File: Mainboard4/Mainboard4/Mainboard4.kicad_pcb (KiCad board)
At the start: 2 copper layers, 145.9 x 180.3 mm, 41 parts, among them J0 Conn_01x18, J1 Conn_01x18, J2 Conn_01x18, J3 Conn_01x18, J4 Conn_01x18, J5 Conn_01x18, J7 Conn_01x02_Female, J8 Conn_01x12_Female, SW1 SW_DIP_x01, SW2 SW_DIP_x01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

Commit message: nearly ok
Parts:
- added C4: 0.1µF, Capacitor_THT:CP_Radial_Tantal_D5.0mm_P2.50mm, F.Cu at (142.4, 46.9)
- added C5: 10µF, Capacitor_THT:CP_Radial_Tantal_D5.0mm_P2.50mm, F.Cu at (137.0, 46.9)
- added J6: Conn_02x08_Odd_Even, Connector_PinHeader_2.54mm:PinHeader_2x08_P2.54mm_Vertical, F.Cu at (191.5, 96.3)
- added JP3: Jumper_2_Open, Connector_PinHeader_2.54mm:PinHeader_1x02_P2.54mm_Vertical, F.Cu at (118.0, 34.0)
- added JP4: Jumper_2_Open, Connector_PinHeader_2.54mm:PinHeader_1x02_P2.54mm_Vertical, F.Cu at (118.0, 38.2)
- added R10: R, Resistor_THT:R_Axial_DIN0207_L6.3mm_D2.5mm_P7.62mm_Horizontal, F.Cu at (191.5, 104.4)
- added R11: R, Resistor_THT:R_Axial_DIN0207_L6.3mm_D2.5mm_P7.62mm_Horizontal, F.Cu at (189.0, 104.4)
- added R12: R, Resistor_THT:R_Axial_DIN0207_L6.3mm_D2.5mm_P7.62mm_Horizontal, F.Cu at (186.4, 104.4)
- added R13: R, Resistor_THT:R_Axial_DIN0207_L6.3mm_D2.5mm_P7.62mm_Horizontal, F.Cu at (183.9, 104.4)
- added R14: R, Resistor_THT:R_Axial_DIN0207_L6.3mm_D2.5mm_P7.62mm_Horizontal, F.Cu at (181.4, 104.4)
- added R15: R, Resistor_THT:R_Axial_DIN0207_L6.3mm_D2.5mm_P7.62mm_Horizontal, F.Cu at (178.8, 104.4)
- added R16: R, Resistor_THT:R_Axial_DIN0207_L6.3mm_D2.5mm_P7.62mm_Horizontal, F.Cu at (176.3, 104.4)
- added R17: R, Resistor_THT:R_Axial_DIN0207_L6.3mm_D2.5mm_P7.62mm_Horizontal, F.Cu at (173.7, 104.4)
- added REF**: MountingHole_2.2mm_M2, MountingHole:MountingHole_2.2mm_M2, F.Cu at (61.0, 38.6)
- added REF**: MountingHole_2.2mm_M2, MountingHole:MountingHole_2.2mm_M2, F.Cu at (101.6, 169.4)
- added REF**: MountingHole_2.2mm_M2, MountingHole:MountingHole_2.2mm_M2, F.Cu at (194.3, 37.6)
- added REF**: MountingHole_2.2mm_M2, MountingHole:MountingHole_2.2mm_M2, F.Cu at (58.4, 206.4)
- added REF**: MountingHole_2.2mm_M2, MountingHole:MountingHole_2.2mm_M2, F.Cu at (102.2, 80.5)
- added REF**: MountingHole_2.2mm_M2, MountingHole:MountingHole_2.2mm_M2, F.Cu at (194.3, 199.4)
- added U7: ULN2803A, Package_DIP:DIP-18_W7.62mm, F.Cu at (191.5, 84.1)
- J_I2C_3: value Conn_01x04_Female -> Conn_01x06_Female; footprint Connector_PinHeader_2.54mm:PinHeader_1x04_P2.54mm_Vertical -> Connector_PinHeader_2.54mm:PinHeader_1x06_P2.54mm_Vertical
- moved C2 55.2 mm to (187.3, 47.2), turned to -90 degrees
- moved R5 38.5 mm to (120.3, 47.1), turned to 0 degrees
- moved JP1 36.5 mm to (189.2, 144.9), turned to 180 degrees
- moved J_POWER1 27.1 mm to (145.0, 34.0), turned to 90 degrees
- moved R9 20.7 mm to (192.7, 164.6)
- moved R2 20.2 mm to (165.1, 46.4), turned to 0 degrees
- moved R8 17.4 mm to (192.5, 150.0), turned to 90 degrees
- moved R4 17.3 mm to (127.9, 43.6), turned to 180 degrees
- moved U1 16.8 mm to (182.2, 42.6)
- moved SW1 14.6 mm to (168.4, 35.1), turned to -90 degrees
- moved C3 13.3 mm to (182.1, 47.2), turned to -90 degrees
- moved JP2 12.5 mm to (189.2, 168.1), turned to 0 degrees
- moved SW3 9.90 mm to (127.3, 34.0), turned to -90 degrees
- moved R3 8.07 mm to (176.5, 50.0), turned to 90 degrees
- moved R6 6.27 mm to (131.1, 49.0), turned to 90 degrees
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- renumbered J7 to J_POWER1
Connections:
- JP2 pad 1: Net-(JP1-Pad1) -> Net-(R9-Pad1)
- JP2 pad 2: Net-(JP2-Pad2) -> Net-(JP1-Pad1)
- J_GUI1 pad 1: unconnected-(J_GUI1-Pad1) -> 12V
- R9 pad 1: Net-(J_BUS1-Pad4) -> Net-(R9-Pad1)
- R9 pad 2: Net-(JP2-Pad2) -> Net-(J_BUS1-Pad4)
- SW3 pad 2: 12V -> Net-(SW3-Pad2)
- U2 pad 48: unconnected-(U2-Pad48) -> LED1
- U2 pad 63: LED4 -> LED8
- U2 pad 79: LED3 -> LED6
- U2 pad 83: unconnected-(U2-Pad83) -> LED5
- U2 pad 85: unconnected-(U2-Pad85) -> LED4
- U2 pad 87: unconnected-(U2-Pad87) -> LED3
- U2 pad 92: unconnected-(U2-Pad92) -> LED2
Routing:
- net 5V: track 133.1 -> 416.8 mm
- net 3V3: track 0.00 -> 234.5 mm, vias 0 -> 1
- net TRACK0_1: track 0.00 -> 125.0 mm
- net TRACK0_0: track 0.00 -> 123.8 mm
- net 12Vunreg: track 0.00 -> 107.9 mm
- net TRACK1_1: track 0.00 -> 103.4 mm
- net TRACK1_0: track 0.00 -> 101.5 mm
- net LED1: track 0.00 -> 82.3 mm
- net TRACK2_1: track 0.00 -> 78.4 mm
- net TRACK2_0: track 0.00 -> 74.1 mm
- net 12V: track 270.8 -> 343.2 mm
- net Net-(JP1-Pad1): track 0.00 -> 55.1 mm
- net TRACK3_1: track 0.00 -> 50.7 mm
- net Net-(J_BUS1-Pad4): track 0.18 -> 50.8 mm
- net TRACK3_0: track 0.00 -> 48.3 mm
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
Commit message: nearly ok
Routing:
- net GND: track 0.00 -> 87.1 mm, vias 0 -> 2
- net 3V3: track 234.5 -> 242.1 mm
- net 5V: track 416.8 -> 413.0 mm, vias 1 -> 2
- net CT0_3: track 85.4 -> 84.0 mm
- net CT1_3: track 48.2 -> 46.9 mm
- net CT5_1: track 125.9 -> 124.8 mm
- net VSENSE4_0: track 162.5 -> 161.7 mm
- net CT5_3: track 122.8 -> 122.0 mm
- net VSENSE3_1: track 136.4 -> 135.7 mm
- net CT0_2: track 64.7 -> 64.1 mm
- net PWM1_1: track 112.9 -> 112.2 mm
- net VSENSE5_0: track 191.7 -> 191.1 mm
- added copper zone on B.Cu, net GND
- added copper zone on F.Cu, net GND

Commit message: nearly ok
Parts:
- moved R10 2.16 mm to (193.7, 104.4)
- moved R17 1.65 mm to (172.1, 104.4)
- moved R11 1.52 mm to (190.5, 104.4)
- moved R16 1.02 mm to (175.3, 104.4)
- moved R12 0.89 mm to (187.3, 104.4)
- moved J_T5 0.64 mm to (183.1, 207.4)
- moved J_T6 0.64 mm to (195.3, 207.4)
- moved J_T1 0.63 mm to (171.4, 207.6)
- moved C2 0.38 mm to (187.7, 47.2)
- moved R15 0.38 mm to (178.4, 104.4)
- moved C4 0.30 mm to (142.7, 46.9)
- moved R13 0.25 mm to (184.2, 104.4)
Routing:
- net GND: track 87.1 -> 68.5 mm, vias 2 -> 0
- net Net-(J_T6-Pad1): track 46.9 -> 43.0 mm
- net 12V: track 343.2 -> 341.3 mm
- net 5V: track 413.0 -> 414.8 mm
- net CT1_3: track 46.9 -> 45.9 mm
- net Net-(J6-Pad2): track 5.59 -> 6.48 mm
- net Net-(J6-Pad16): track 5.59 -> 6.27 mm
- net Net-(J_T6-Pad3): track 39.3 -> 38.7 mm
- net Net-(J6-Pad4): track 5.59 -> 6.22 mm

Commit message: ..
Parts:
- moved C2 2.92 mm to (190.6, 47.2)
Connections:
- C1 pad 2: 5V -> 5VCPU
- C3 pad 1: Net-(R3-Pad1) -> 5V
- R3 pad 1: Net-(R3-Pad1) -> 5V
- SW1 pad 1: Net-(R3-Pad1) -> 5V
- SW1 pad 2: 5V -> 5VCPU
- U1 pad 2: Net-(R3-Pad1) -> 5V
- U2 pad 49: 5V -> 5VCPU
- U2 pad 50: 5V -> 5VCPU
- U2 pad 51: 5V -> 5VCPU
- U2 pad 52: 5V -> 5VCPU
- U4 pad 3: 5V -> 5VCPU
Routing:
- net 5VCPU: track 0.00 -> 194.8 mm, vias 0 -> 1
- net 5V: track 414.8 -> 222.3 mm, vias 2 -> 0
- net Net-(R3-Pad1): track 32.8 -> 0.00 mm
- net 12Vunreg: track 108.2 -> 109.8 mm

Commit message: mainboard4 ready for production
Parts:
- moved SW_12V1 28.7 mm to (98.6, 34.3)
- moved C2 18.3 mm to (172.3, 45.9)
- moved C5 18.3 mm to (118.7, 45.7)
- moved J_BUS1 18.3 mm to (178.1, 173.7)
- moved J_GUI1 18.3 mm to (178.1, 150.9)
- moved J_I2C_3_IUI1 18.3 mm to (178.1, 118.6)
- moved J_T1 18.3 mm to (153.1, 206.4)
- moved J_T2 18.3 mm to (139.8, 206.4)
- moved R1 18.3 mm to (154.4, 41.5)
- moved R10 18.3 mm to (175.4, 103.1)
- moved R11 18.3 mm to (172.2, 103.1)
- moved R13 18.3 mm to (165.9, 103.1)
- moved R15 18.3 mm to (160.1, 103.1)
- moved R17 18.3 mm to (153.8, 103.1)
- moved R3 18.3 mm to (158.2, 48.8)
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- renumbered J6 to J6_LEDS1, J_I2C_3 to J_I2C_3_IUI1, SW3 to SW_12V1, SW1 to SW_5VCPU1, SW2 to SW_GEN1
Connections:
- C5 pad 1: Net-(R6-Pad1) -> Net-(C5-Pad1)
- JP3 pad 1: Net-(SW3-Pad2) -> Net-(C5-Pad1)
- JP3 pad 2: 12V -> Net-(JP3-Pad2)
- JP4 pad 2: 12V -> Net-(JP3-Pad2)
- R6 pad 1: Net-(R6-Pad1) -> Net-(C5-Pad1)
- SW_12V1 pad 1: Net-(R6-Pad1) -> Net-(JP3-Pad2)
- SW_12V1 pad 2: Net-(SW3-Pad2) -> 12V
- U3 pad 2: Net-(R6-Pad1) -> Net-(C5-Pad1)
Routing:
- net Net-(C5-Pad1): track 0.00 -> 34.2 mm
- net Net-(R6-Pad1): track 29.5 -> 0.00 mm
- net 12Vunreg: track 109.8 -> 98.2 mm
- net Net-(JP3-Pad2): track 0.00 -> 11.2 mm
- net Net-(SW3-Pad2): track 6.73 -> 0.00 mm
- net 12V: track 341.3 -> 338.3 mm
- net 5VCPU: track 194.8 -> 195.3 mm
- net GND: vias 0 -> 3
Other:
- board text added: "Z-ATC Mainboard v0.4 © D. Braun 2022"
- board text removed: "Mainboard v0.4 © D. Braun 2022"

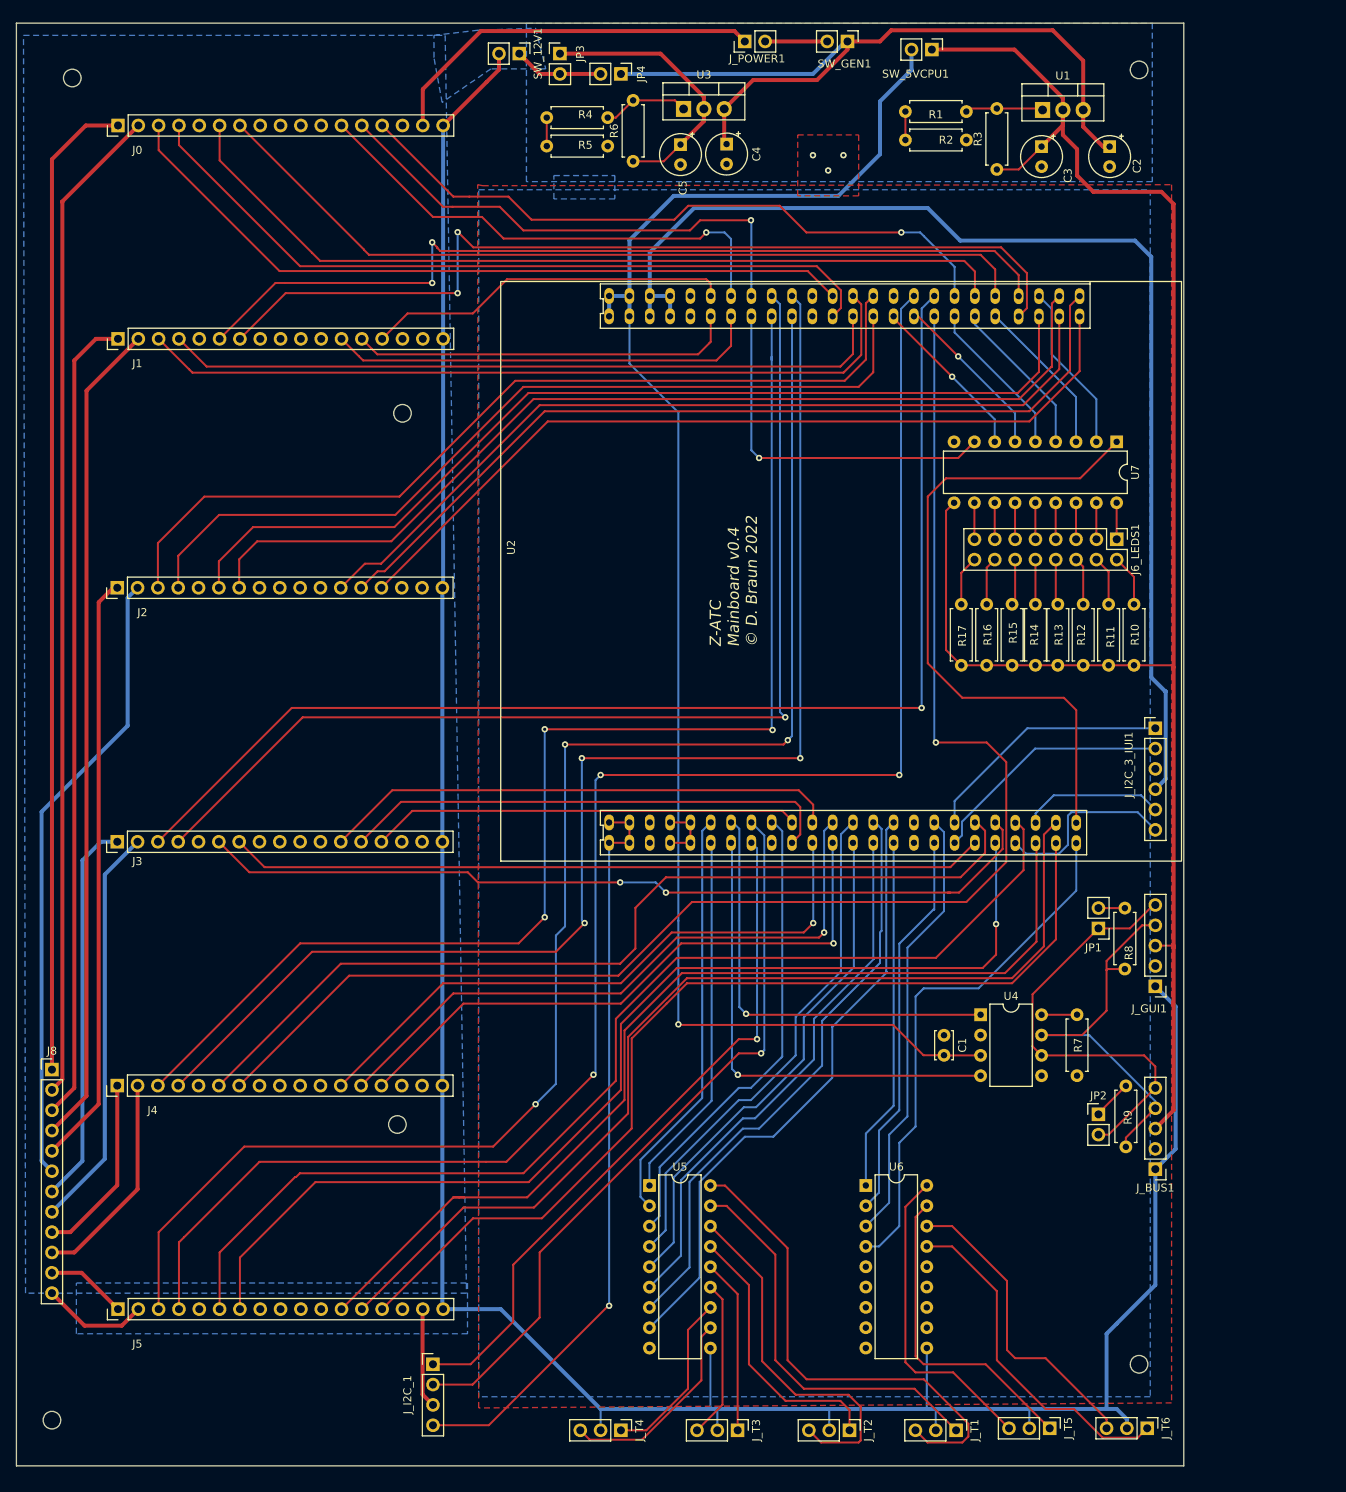
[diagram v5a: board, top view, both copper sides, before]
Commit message: updated to have full USB and external flash
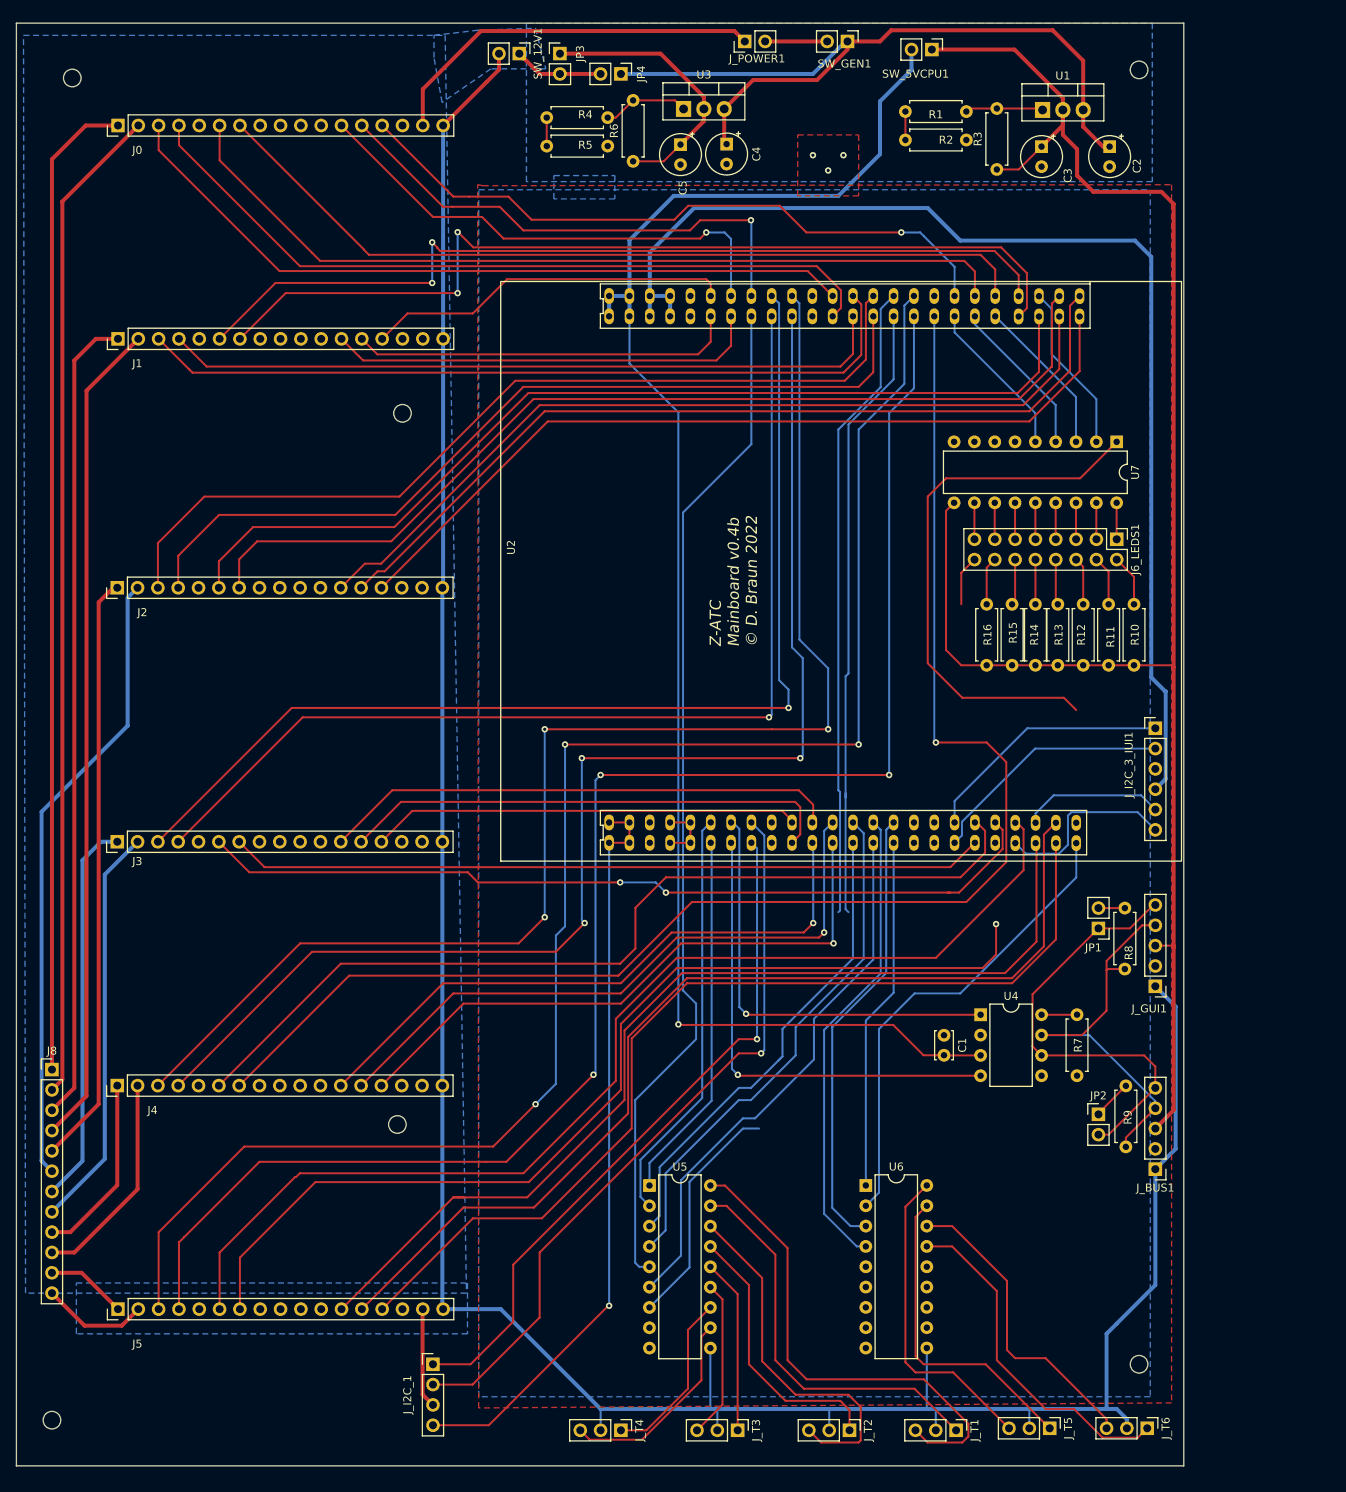
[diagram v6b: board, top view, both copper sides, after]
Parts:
- removed R17: R, Resistor_THT:R_Axial_DIN0207_L6.3mm_D2.5mm_P7.62mm_Horizontal
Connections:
- net SWO renamed SWO_SPI1_SCK
- J6_LEDS1 pad 15: Net-(J6_LEDS1-Pad15) -> unconnected-(J6_LEDS1-Pad15)
- J6_LEDS1 pad 16: Net-(J6_LEDS1-Pad16) -> unconnected-(J6_LEDS1-Pad16)
- U2 pad 18: TURN2A -> SPI1_MOSI
- U2 pad 25: TURN3A -> TURN2A
- U2 pad 28: TURN4A -> TURN6B
- U2 pad 30: TURN4B -> TURN6A
- U2 pad 33: TURN5B -> usb_vbus
- U2 pad 34: TURN6A -> usb_otg_id
- U2 pad 47: TURN6B -> TURN5B
- U2 pad 63: LED8 -> TURN3A
- U2 pad 65: VSENSE4_0 -> VSENSE3_1
- U2 pad 66: VSENSE3_1 -> VSENSE3_0
- U2 pad 67: VSENSE5_0 -> VSENSE4_1
- U2 pad 68: VSENSE4_1 -> VSENSE4_0
- U2 pad 77: BOARD_LED2 -> TURN4B
- U2 pad 78: BOARD_LED -> TURN4A
- U2 pad 79: LED6 -> VSENSE5_1
- U2 pad 80: VSENSE5_1 -> VSENSE5_0
- U2 pad 82: VSENSE3_0 -> flash_cs
- U7 pad 11: Net-(J6_LEDS1-Pad15) -> unconnected-(U7-Pad11)
- U7 pad 7: BOARD_LED2 -> LED7
- U7 pad 8: LED8 -> unconnected-(U7-Pad8)
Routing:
- net TURN3A: track 64.6 -> 127.2 mm
- net LED8: track 45.9 -> 0.00 mm, vias 1 -> 0
- net TURN4A: track 74.3 -> 109.3 mm
- net LED6: track 21.2 -> 0.00 mm, vias 1 -> 0
- net BOARD_LED2: track 20.9 -> 0.00 mm, vias 1 -> 0
- net VSENSE3_0: track 154.5 -> 138.1 mm
- net VSENSE5_0: track 191.1 -> 205.5 mm
- net LED1: track 82.3 -> 68.3 mm
- net TURN5B: track 49.0 -> 59.6 mm
- net VSENSE4_0: track 161.7 -> 172.0 mm
- net PWM5_2: track 135.6 -> 125.3 mm
- net TURN6B: track 66.3 -> 59.1 mm
- net unconnected-(J6_LEDS1-Pad16): track 0.00 -> 6.27 mm
- net Net-(J6_LEDS1-Pad16): track 6.27 -> 0.00 mm
- net VSENSE3_1: track 135.7 -> 130.6 mm
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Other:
- board text added: "Z-ATC Mainboard v0.4b © D. Braun 2022"
- board text removed: "Z-ATC Mainboard v0.4 © D. Braun 2022"

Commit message: updated to have full USB and external flash
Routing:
- net TURN4B: track 77.9 -> 143.3 mm, vias 0 -> 1
- net TURN4A: track 109.3 -> 140.8 mm, vias 0 -> 1
- net LED1: track 68.3 -> 82.1 mm
- net PWM5_2: track 125.3 -> 135.5 mm
- net TURN2B: track 65.6 -> 74.7 mm
- net TURN2A: track 60.0 -> 68.5 mm
- net TURN3B: track 68.0 -> 76.4 mm
- net unconnected-(J6_LEDS1-Pad16): track 6.27 -> 0.00 mm
- net unconnected-(U7-Pad11): track 4.57 -> 0.00 mm
- net TURN6A: track 57.8 -> 55.5 mm

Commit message: ..
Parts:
- moved R16 0.64 mm to (156.3, 103.1)
- moved R15 0.63 mm to (159.5, 103.1)
- moved R14 0.38 mm to (162.7, 103.1)
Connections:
- net TURN4A renamed BOARD_LED
- net TURN4B renamed BOARD_LED2
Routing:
- net GND: track 68.5 -> 20.1 mm, vias 3 -> 7
- net 5VCPU: track 195.3 -> 197.3 mm
- net 5V: track 222.3 -> 220.4 mm
- net CT5_1: track 124.8 -> 123.4 mm
